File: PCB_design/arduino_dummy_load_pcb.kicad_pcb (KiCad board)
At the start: 2 copper layers, 209.6 x 109.2 mm, 115 parts, among them J1 Barrel_Jack, J2 Conn_02x08_Odd_Even, J3 Conn_01x01, U1 MCP3208

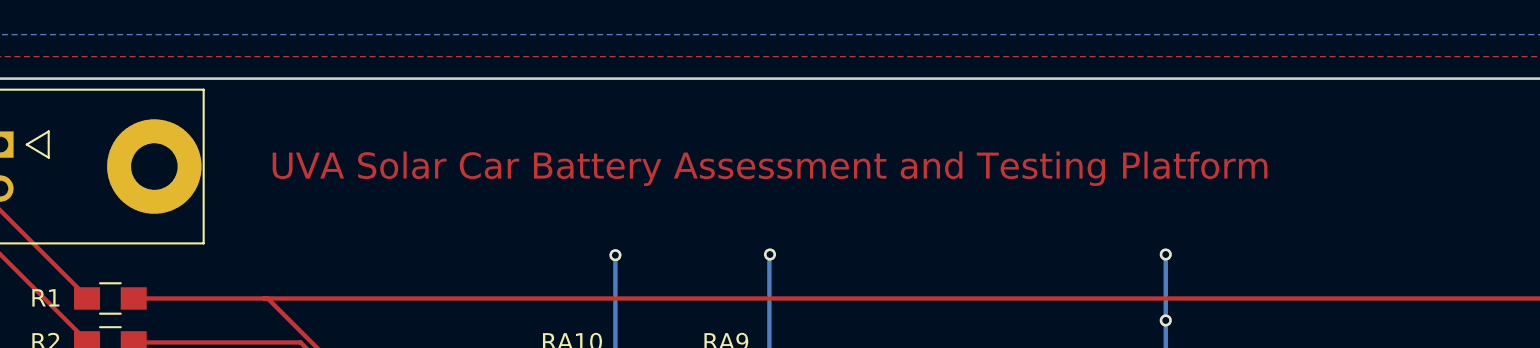
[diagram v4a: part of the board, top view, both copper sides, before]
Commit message: Removed text on copper Bottom
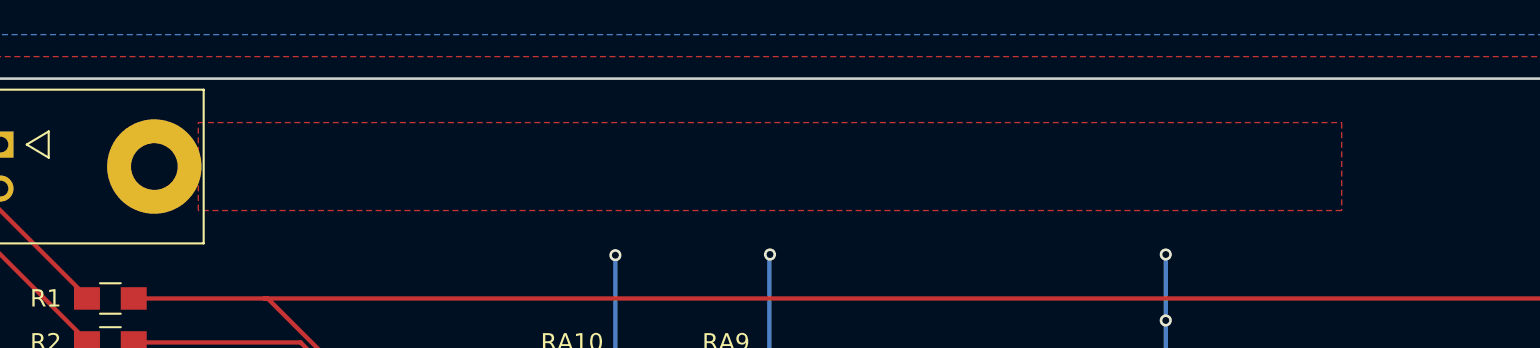
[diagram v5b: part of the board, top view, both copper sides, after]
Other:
- board text removed: "UVA Solar Car Battery Assessment and Testing Platform"
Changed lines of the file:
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@@
   (general
     (links 259)
-    (no_connects 0)
+    (no_connects 6)
     (area 43.914287 30.439405 267.970001 149.860001)
     (thickness 1.6)
-    (drawings 11)
+    (drawings 10)
     (tracks 609)
     (zones 0)
@@
   (page A4)
   (layers
-    (0 F.Cu signal hide)
-    (31 B.Cu signal)
+    (0 F.Cu signal)
+    (31 B.Cu signal hide)
     (32 B.Adhes user)
     (33 F.Adhes user)
@@
     (effects (font (size 3 3) (thickness 0.3)))
   )
-  (gr_text "UVA Solar Car Battery Assessment and Testing Platform" (at 132.08 43.18) (layer F.Cu)
-    (effects (font (size 1.5 1.5) (thickness 0.3)))
-  )
   (dimension 109.22 (width 0.3) (layer Margin)
     (gr_text "4.3000 in" (at 49.45 92.71 90) (layer Margin)
@@
   (gr_line (start 55.88 147.32) (end 265.43 147.32) (layer Edge.Cuts) (width 0.15))
   (gr_line (start 55.88 38.1) (end 55.88 147.32) (layer Edge.Cuts) (width 0.15))
+  (segment (start 71.12 44.45) (end 71.129574 44.45) (width 0.25) (layer F.Cu) (net 0) (status 30))
+  (segment (start 71.135349 44.465349) (end 71.12 44.45) (width 0.25) (layer F.Cu) (net 0) (status 30))
   (segment (start 78.23794 71.716694) (end 78.23794 72.211668) (width 0.25) (layer F.Cu) (net 1))
   (segment (start 78.23794 70.82705) (end 78.23794 71.716694) (width 0.25) (layer F.Cu) (net 1))
@@
   (segment (start 75.772319 78.312319) (end 75.772319 93.967681) (width 1.27) (layer B.Cu) (net 57))
   (segment (start 75.772319 93.967681) (end 59.57 110.17) (width 1.27) (layer B.Cu) (net 57))
-  (segment (start 71.12 44.45) (end 71.129574 44.45) (width 0.25) (layer F.Cu) (net 58) (status 30))
-  (segment (start 71.135349 44.465349) (end 71.12 44.45) (width 0.25) (layer F.Cu) (net 58) (status 30))
   (segment (start 80.01 53.34) (end 62.23 53.34) (width 0.25) (layer B.Cu) (net 59))
   (segment (start 82.11462 53.34) (end 80.01 53.34) (width 0.25) (layer F.Cu) (net 59))
@@
       )
     )
+  )
+  (zone (net 1) (net_name +5V) (layer F.Cu) (hatch edge 0.508)
+    (connect_pads (clearance 0.508))
+    (min_thickness 0.254)
+    (fill yes (arc_segments 16) (thermal_gap 0.508) (thermal_bridge_width 0.508))
+    (polygon
+      (pts
+        (xy 165.1 40.64) (xy 165.1 45.72) (xy 99.06 45.72) (xy 99.06 40.64)
+      )
+    )

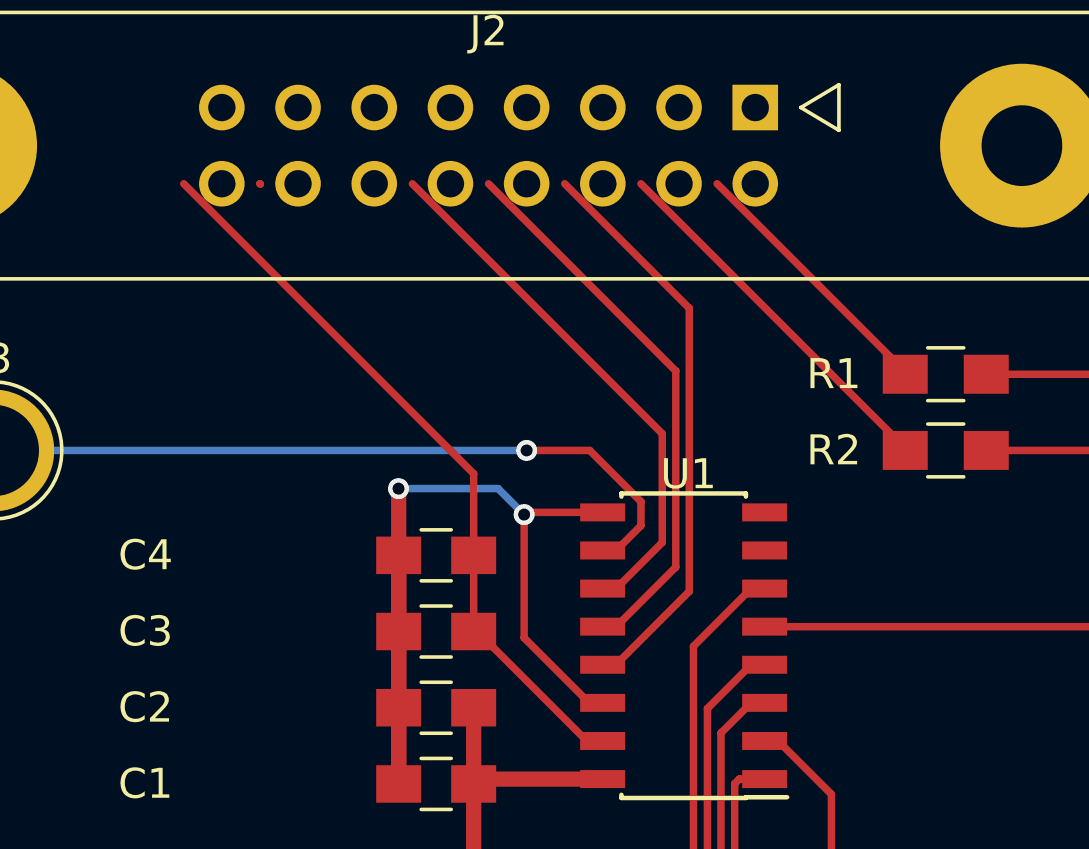
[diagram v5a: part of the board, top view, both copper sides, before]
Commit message: Re-routed traces that were broken by moving components away from corner
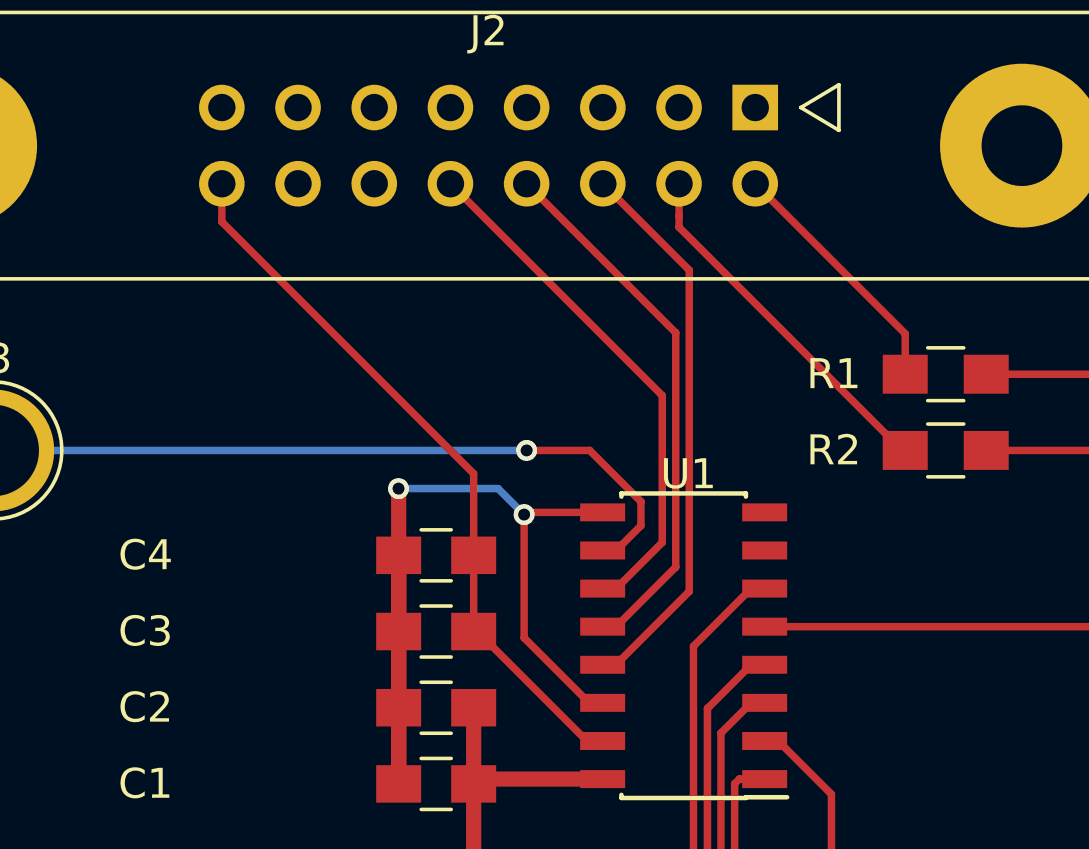
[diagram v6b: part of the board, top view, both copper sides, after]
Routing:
- net Net-(J2-Pad8): track 18.6 -> 18.1 mm
- net Net-(J2-Pad10): track 18.0 -> 17.5 mm
- net VREF: track 24.7 -> 24.2 mm
- net Net-(J2-Pad6): track 19.2 -> 18.7 mm
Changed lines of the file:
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@@
   (general
     (links 259)
-    (no_connects 6)
+    (no_connects 0)
     (area 43.914287 30.439405 267.970001 149.860001)
     (thickness 1.6)
     (drawings 10)
-    (tracks 609)
+    (tracks 612)
     (zones 0)
     (modules 115)
@@
   (page A4)
   (layers
-    (0 F.Cu signal)
-    (31 B.Cu signal hide)
+    (0 F.Cu signal hide)
+    (31 B.Cu signal)
     (32 B.Adhes user)
     (33 F.Adhes user)
@@
   (gr_line (start 55.88 147.32) (end 265.43 147.32) (layer Edge.Cuts) (width 0.15))
   (gr_line (start 55.88 38.1) (end 55.88 147.32) (layer Edge.Cuts) (width 0.15))
-  (segment (start 71.12 44.45) (end 71.129574 44.45) (width 0.25) (layer F.Cu) (net 0) (status 30))
-  (segment (start 71.135349 44.465349) (end 71.12 44.45) (width 0.25) (layer F.Cu) (net 0) (status 30))
   (segment (start 78.23794 71.716694) (end 78.23794 72.211668) (width 0.25) (layer F.Cu) (net 1))
   (segment (start 78.23794 70.82705) (end 78.23794 71.716694) (width 0.25) (layer F.Cu) (net 1))
@@
   (segment (start 219.528546 81.579034) (end 219.528546 82.029034) (width 0.25) (layer F.Cu) (net 14) (status 30))
   (segment (start 125.548546 82.029034) (end 125.548546 81.579034) (width 0.25) (layer F.Cu) (net 14) (status 30))
-  (segment (start 84.53069 52.78069) (end 76.2 44.45) (width 0.25) (layer F.Cu) (net 16) (status 20))
-  (segment (start 82.543718 57.9441) (end 82.993718 57.9441) (width 0.25) (layer F.Cu) (net 16) (status 30))
-  (segment (start 84.53069 56.407128) (end 84.53069 52.78069) (width 0.25) (layer F.Cu) (net 16))
-  (segment (start 82.993718 57.9441) (end 84.53069 56.407128) (width 0.25) (layer F.Cu) (net 16) (status 10))
+  (segment (start 82.543718 57.9441) (end 82.993718 57.9441) (width 0.25) (layer F.Cu) (net 16))
+  (segment (start 82.993718 57.9441) (end 84.53069 56.407128) (width 0.25) (layer F.Cu) (net 16))
+  (segment (start 84.53069 56.407128) (end 84.53069 51.51069) (width 0.25) (layer F.Cu) (net 16))
+  (segment (start 84.53069 51.51069) (end 77.47 44.45) (width 0.25) (layer F.Cu) (net 16))
   (segment (start 160.02 111.76) (end 159.369516 112.410484) (width 0.25) (layer F.Cu) (net 17) (status 10))
   (segment (start 84.425023 89.605023) (end 82.55 87.73) (width 0.25) (layer F.Cu) (net 17) (status 20))
@@
   (segment (start 222.388546 81.709034) (end 222.068546 82.029034) (width 0.25) (layer F.Cu) (net 29) (status 20))
   (segment (start 224.608546 81.709034) (end 222.388546 81.709034) (width 0.25) (layer F.Cu) (net 29) (status 10))
-  (segment (start 86.36 44.45) (end 92.63 50.72) (width 0.25) (layer F.Cu) (net 30) (status 30))
+  (segment (start 92.63 50.8) (end 92.63 49.45) (width 0.25) (layer F.Cu) (net 30))
+  (segment (start 92.63 49.45) (end 87.63 44.45) (width 0.25) (layer F.Cu) (net 30))
   (segment (start 92.63 50.72) (end 92.63 50.8) (width 0.25) (layer F.Cu) (net 30) (status 30))
-  (segment (start 83.82 44.45) (end 92.63 53.26) (width 0.25) (layer F.Cu) (net 31) (status 30))
+  (segment (start 92.63 53.34) (end 92.53 53.34) (width 0.25) (layer F.Cu) (net 31))
+  (segment (start 92.53 53.34) (end 85.09 45.9) (width 0.25) (layer F.Cu) (net 31))
+  (segment (start 85.09 45.9) (end 85.09 45.524802) (width 0.25) (layer F.Cu) (net 31))
+  (segment (start 85.09 45.524802) (end 85.09 44.45) (width 0.25) (layer F.Cu) (net 31))
   (segment (start 92.63 53.26) (end 92.63 53.34) (width 0.25) (layer F.Cu) (net 31) (status 30))
-  (segment (start 81.28 44.45) (end 85.430712 48.600712) (width 0.25) (layer F.Cu) (net 32) (status 10))
-  (segment (start 85.430712 48.600712) (end 85.430712 58.038896) (width 0.25) (layer F.Cu) (net 32))
-  (segment (start 85.430712 58.038896) (end 82.985508 60.4841) (width 0.25) (layer F.Cu) (net 32) (status 20))
-  (segment (start 82.985508 60.4841) (end 82.543718 60.4841) (width 0.25) (layer F.Cu) (net 32) (status 30))
-  (segment (start 84.980701 57.227117) (end 82.993718 59.2141) (width 0.25) (layer F.Cu) (net 33) (status 20))
-  (segment (start 78.74 44.45) (end 84.980701 50.690701) (width 0.25) (layer F.Cu) (net 33) (status 10))
-  (segment (start 82.993718 59.2141) (end 82.543718 59.2141) (width 0.25) (layer F.Cu) (net 33) (status 30))
-  (segment (start 84.980701 50.690701) (end 84.980701 57.227117) (width 0.25) (layer F.Cu) (net 33))
-  (segment (start 68.58 44.45) (end 78.2441 54.1141) (width 0.25) (layer F.Cu) (net 34))
+  (segment (start 82.543718 60.4841) (end 82.985508 60.4841) (width 0.25) (layer F.Cu) (net 32))
+  (segment (start 82.985508 60.4841) (end 85.430712 58.038896) (width 0.25) (layer F.Cu) (net 32))
+  (segment (start 85.430712 58.038896) (end 85.430712 47.330712) (width 0.25) (layer F.Cu) (net 32))
+  (segment (start 85.430712 47.330712) (end 82.55 44.45) (width 0.25) (layer F.Cu) (net 32))
+  (segment (start 82.543718 59.2141) (end 82.993718 59.2141) (width 0.25) (layer F.Cu) (net 33))
+  (segment (start 82.993718 59.2141) (end 84.980701 57.227117) (width 0.25) (layer F.Cu) (net 33))
+  (segment (start 84.980701 49.420701) (end 80.01 44.45) (width 0.25) (layer F.Cu) (net 33))
+  (segment (start 84.980701 57.227117) (end 84.980701 49.420701) (width 0.25) (layer F.Cu) (net 33))
+  (segment (start 69.85 44.45) (end 69.85 45.72) (width 0.25) (layer F.Cu) (net 34))
+  (segment (start 69.85 45.72) (end 78.2441 54.1141) (width 0.25) (layer F.Cu) (net 34))
   (segment (start 78.2441 54.1141) (end 78.2441 56.836282) (width 0.25) (layer F.Cu) (net 34))
   (segment (start 78.2441 59.376282) (end 78.2441 56.836282) (width 0.25) (layer F.Cu) (net 34) (status 30))
